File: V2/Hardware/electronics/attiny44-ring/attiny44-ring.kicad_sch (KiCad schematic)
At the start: 16 parts, among them J1 CHAIN_IN, J2 CHAIN_OUT, J3 28BYJ-48, J4 HOME_SENSOR, J5 AVR_ISP_2X3, J6 5V_INJECT, U1 ATtiny44A-SS, U2 ULN2003A

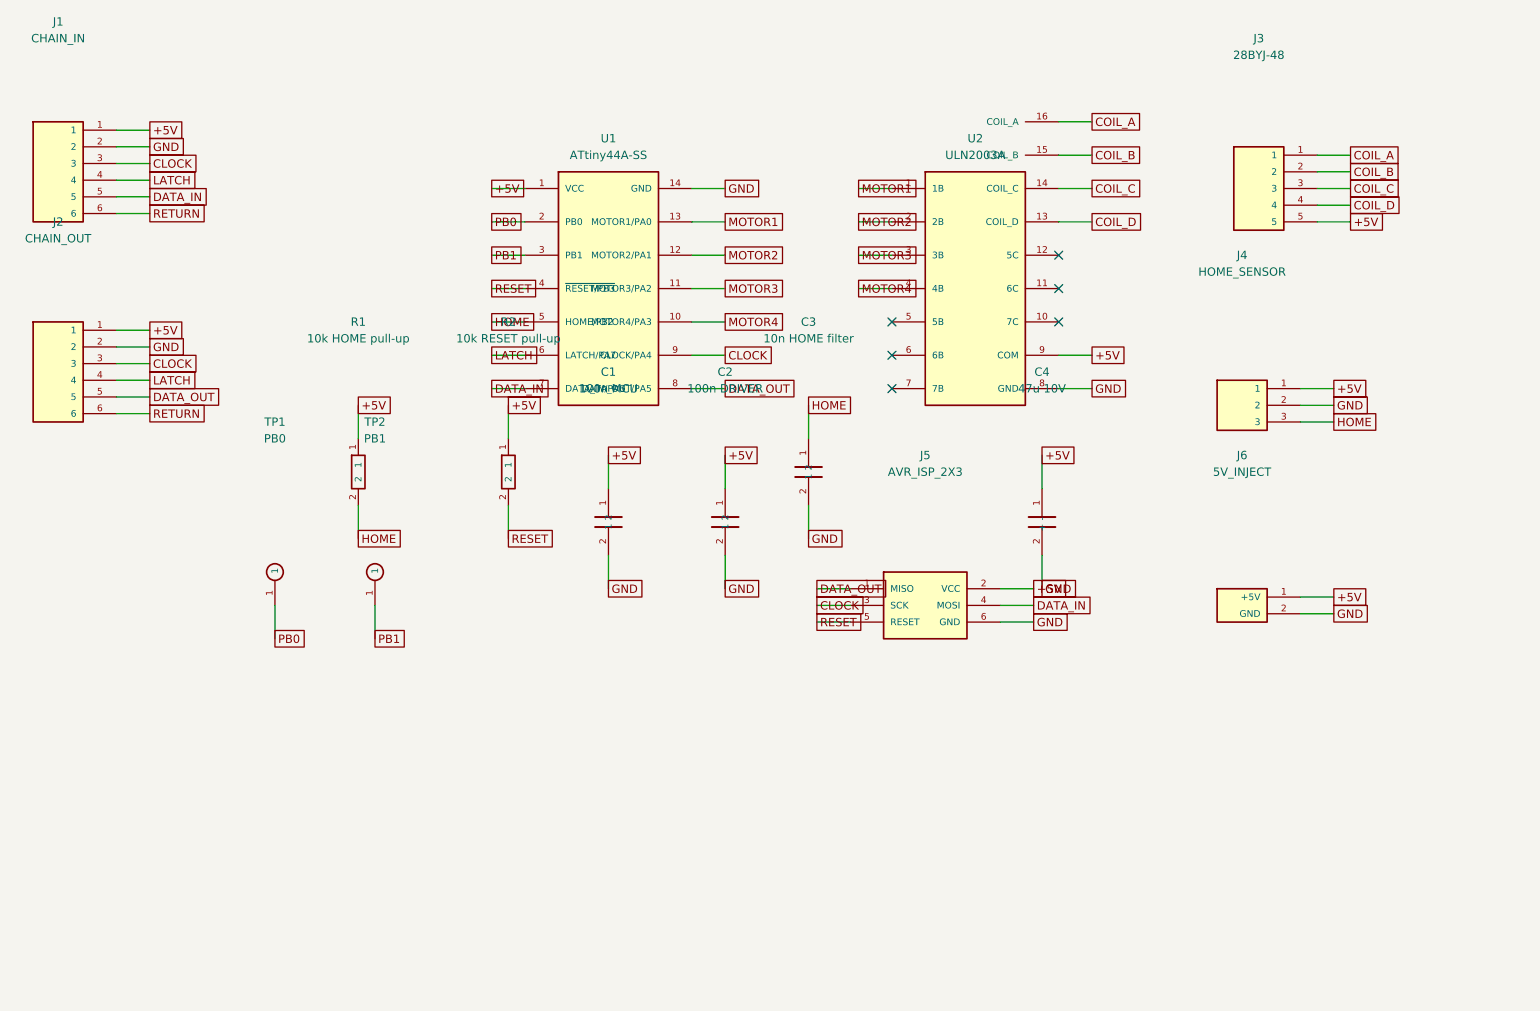
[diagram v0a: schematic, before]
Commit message: Redesign ATtiny44 ring board for milling
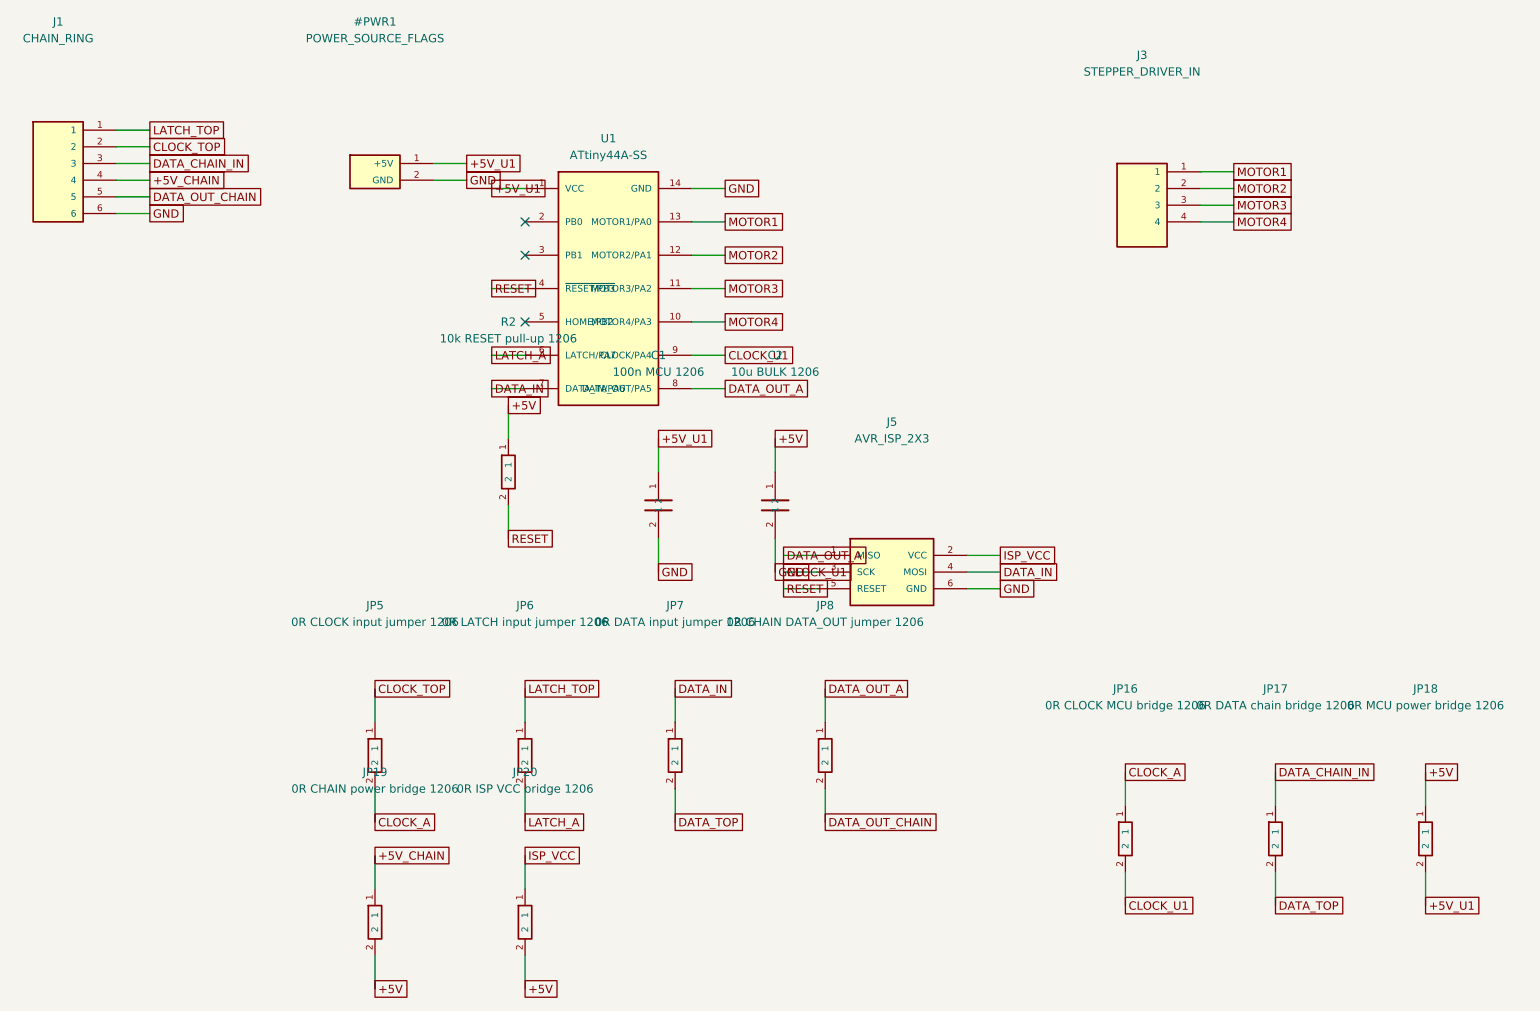
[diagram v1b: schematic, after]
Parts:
- removed C3: 10n HOME filter, Capacitor_SMD:C_0805_2012Metric_Pad1.18x1.45mm_HandSolder, symbol attiny44-ring:C
- removed C4: 47u 10V, Capacitor_THT:CP_Radial_D5.0mm_P2.00mm, symbol attiny44-ring:CP
- removed J2: CHAIN_OUT, Connector_JST:JST_XH_B6B-XH-A_1x06_P2.50mm_Vertical, symbol attiny44-ring:CONN6
- removed J4: HOME_SENSOR, Connector_JST:JST_XH_B3B-XH-A_1x03_P2.50mm_Vertical, symbol attiny44-ring:CONN3
- removed J6: 5V_INJECT, Connector_JST:JST_XH_B2B-XH-A_1x02_P2.50mm_Vertical, symbol attiny44-ring:CONN2
- removed R1: 10k HOME pull-up, Resistor_SMD:R_0805_2012Metric_Pad1.20x1.40mm_HandSolder, symbol attiny44-ring:R
- removed TP1: PB0, TestPoint:TestPoint_Plated_Hole_D2.0mm, symbol attiny44-ring:TESTPOINT
- removed TP2: PB1, TestPoint:TestPoint_Plated_Hole_D2.0mm, symbol attiny44-ring:TESTPOINT
- removed U2: ULN2003A, Package_SO:SOIC-16_3.9x9.9mm_P1.27mm, symbol attiny44-ring:ULN2003A
- added #PWR1: POWER_SOURCE_FLAGS, symbol attiny44-ring:CONN2
- added JP16: 0R CLOCK MCU bridge 1206, Resistor_SMD:R_1206_3216Metric_Pad1.30x1.75mm_HandSolder, symbol attiny44-ring:R
- added JP17: 0R DATA chain bridge 1206, Resistor_SMD:R_1206_3216Metric_Pad1.30x1.75mm_HandSolder, symbol attiny44-ring:R
- added JP18: 0R MCU power bridge 1206, Resistor_SMD:R_1206_3216Metric_Pad1.30x1.75mm_HandSolder, symbol attiny44-ring:R
- added JP19: 0R CHAIN power bridge 1206, Resistor_SMD:R_1206_3216Metric_Pad1.30x1.75mm_HandSolder, symbol attiny44-ring:R
- added JP20: 0R ISP VCC bridge 1206, Resistor_SMD:R_1206_3216Metric_Pad1.30x1.75mm_HandSolder, symbol attiny44-ring:R
- added JP5: 0R CLOCK input jumper 1206, Resistor_SMD:R_1206_3216Metric_Pad1.30x1.75mm_HandSolder, symbol attiny44-ring:R
- added JP6: 0R LATCH input jumper 1206, Resistor_SMD:R_1206_3216Metric_Pad1.30x1.75mm_HandSolder, symbol attiny44-ring:R
- added JP7: 0R DATA input jumper 1206, Resistor_SMD:R_1206_3216Metric_Pad1.30x1.75mm_HandSolder, symbol attiny44-ring:R
- added JP8: 0R CHAIN DATA_OUT jumper 1206, Resistor_SMD:R_1206_3216Metric_Pad1.30x1.75mm_HandSolder, symbol attiny44-ring:R
- C1: value 100n MCU -> 100n MCU 1206; footprint Capacitor_SMD:C_0805_2012Metric_Pad1.18x1.45mm_HandSolder -> Capacitor_SMD:C_1206_3216Metric_Pad1.33x1.80mm_HandSolder
- C2: value 100n DRIVER -> 10u BULK 1206; footprint Capacitor_SMD:C_0805_2012Metric_Pad1.18x1.45mm_HandSolder -> Capacitor_SMD:C_1206_3216Metric_Pad1.33x1.80mm_HandSolder
- J1: value CHAIN_IN -> CHAIN_RING; footprint Connector_JST:JST_XH_B6B-XH-A_1x06_P2.50mm_Vertical -> Connector_PinHeader_2.54mm:PinHeader_2x03_P2.54mm_Vertical_SMD
- J3: value 28BYJ-48 -> STEPPER_DRIVER_IN; footprint Connector_JST:JST_XH_B5B-XH-A_1x05_P2.50mm_Vertical -> Connector_PinHeader_2.54mm:PinHeader_1x04_P2.54mm_Vertical_SMD_Pin1Left; symbol attiny44-ring:CONN5 -> attiny44-ring:CONN4
- J5: footprint Connector_IDC:IDC-Header_2x03_P2.54mm_Vertical -> Connector_PinHeader_2.54mm:PinHeader_2x03_P2.54mm_Vertical_SMD
- R2: value 10k RESET pull-up -> 10k RESET pull-up 1206; footprint Resistor_SMD:R_0805_2012Metric_Pad1.20x1.40mm_HandSolder -> Resistor_SMD:R_1206_3216Metric_Pad1.30x1.75mm_HandSolder
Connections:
- net COIL_A is gone; now on net MOTOR1: J3.1
- net COIL_B is gone; now on net MOTOR2: J3.2
- net COIL_C is gone; now on net MOTOR3: J3.3
- net COIL_D is gone; now on net MOTOR4: J3.4
- net RETURN is gone; now on net GND: J1.6
- net +5V: now also JP18.1, JP19.2, JP20.2; no longer C1.1, J1.1, J3.5, J5.2 (VCC), U1.1 (VCC)
- net DATA_IN: now also JP7.1; no longer J1.5
- net GND: now also #PWR1.2 (GND); no longer J1.2
- net CLOCK renamed CLOCK_U1
- net CLOCK_U1: now also JP16.2; no longer J1.3
- net DATA_OUT renamed DATA_OUT_A
- net DATA_OUT_A: now also JP8.1
- net HOME: no longer names the net of U1.5 (HOME/PB2)
- net LATCH renamed +5V_CHAIN
- net +5V_CHAIN: now also JP19.1; no longer U1.6 (LATCH/PA7)
- net PB0: no longer names the net of U1.2 (PB0)
- net PB1: no longer names the net of U1.3 (PB1)
- new net +5V_U1: #PWR1.1 (+5V), C1.1, JP18.2, U1.1 (VCC)
- new net CLOCK_A: JP16.1, JP5.2
- new net CLOCK_TOP: J1.2, JP5.1
- new net DATA_CHAIN_IN: J1.3, JP17.1
- new net DATA_OUT_CHAIN: J1.5, JP8.2
- new net DATA_TOP: JP17.2, JP7.2
- new net ISP_VCC: J5.2 (VCC), JP20.1
- new net LATCH_A: JP6.2, U1.6 (LATCH/PA7)
- new net LATCH_TOP: J1.1, JP6.1
- no-connect marks 6 -> 3
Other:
- title: Alphabets V2 ATtiny44 SPI ring module -> Alphabets V2 ATtiny44 millable ring module
- moved on the sheet: C1, C2, J5

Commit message: Compact ATtiny44 ring PCB to 50x57 mm
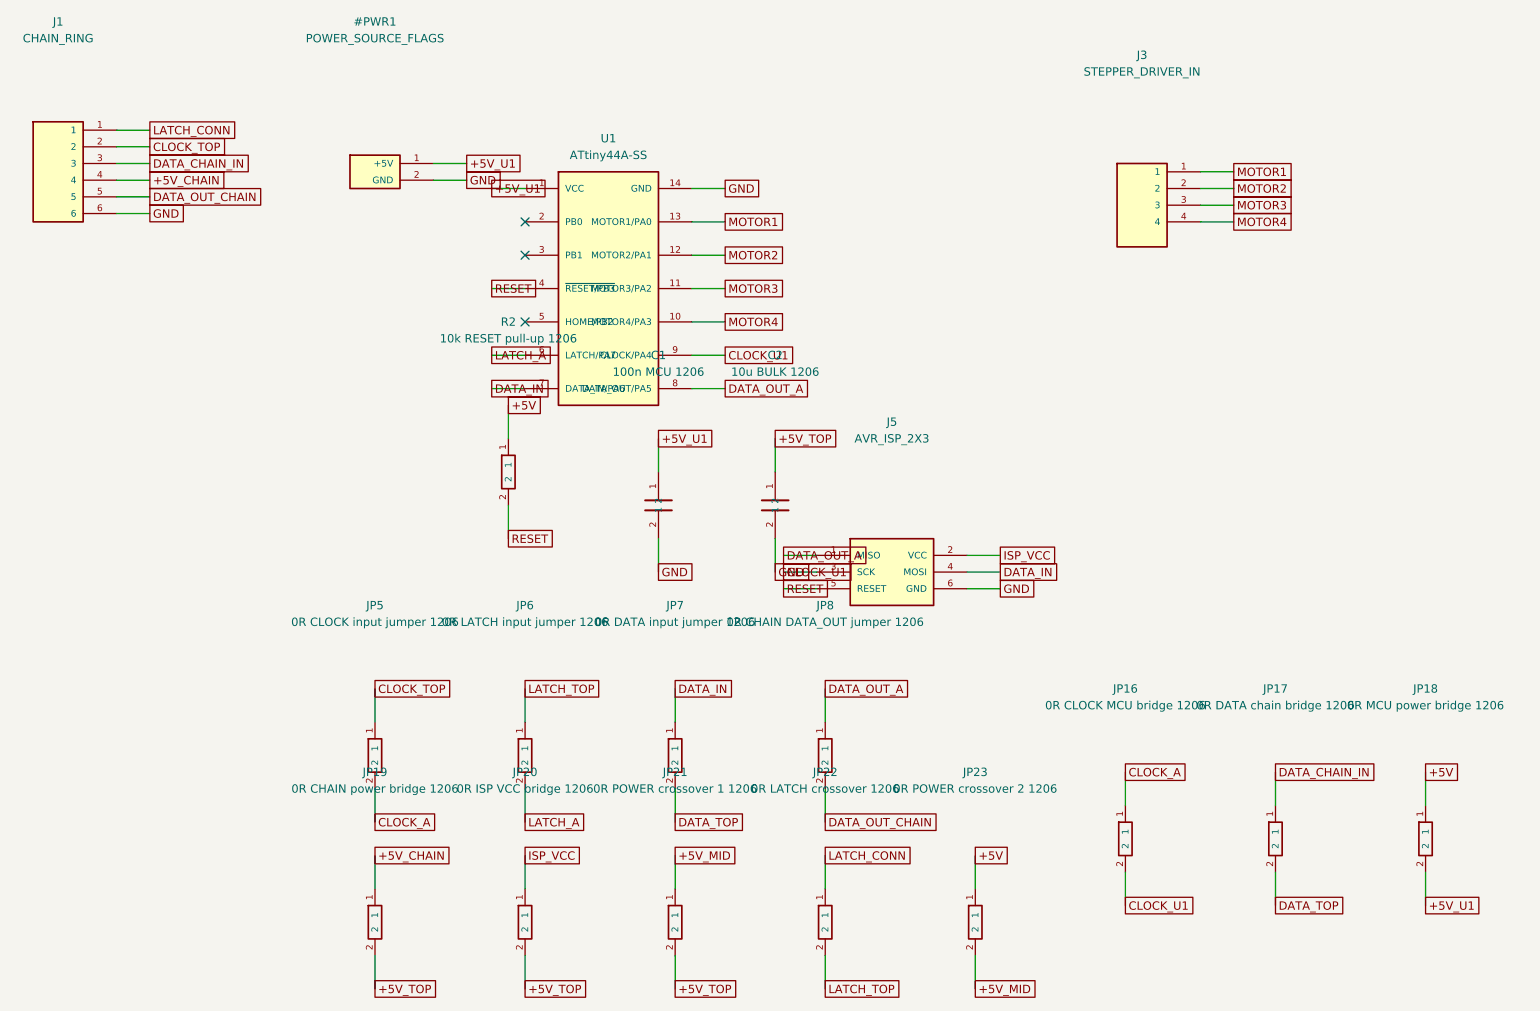
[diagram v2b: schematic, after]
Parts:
- added JP21: 0R POWER crossover 1 1206, Alphabets:R_1206_3216Metric_CompactCrossover, symbol attiny44-ring:R
- added JP22: 0R LATCH crossover 1206, Alphabets:R_1206_3216Metric_CompactCrossover, symbol attiny44-ring:R
- added JP23: 0R POWER crossover 2 1206, Alphabets:R_1206_3216Metric_CompactCrossover, symbol attiny44-ring:R
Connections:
- net +5V: now also JP23.1; no longer C2.1, JP19.2, JP20.2
- net LATCH_TOP: now also JP22.2; no longer J1.1
- new net +5V_MID: JP21.1, JP23.2
- new net +5V_TOP: C2.1, JP19.2, JP20.2, JP21.2
- new net LATCH_CONN: J1.1, JP22.1

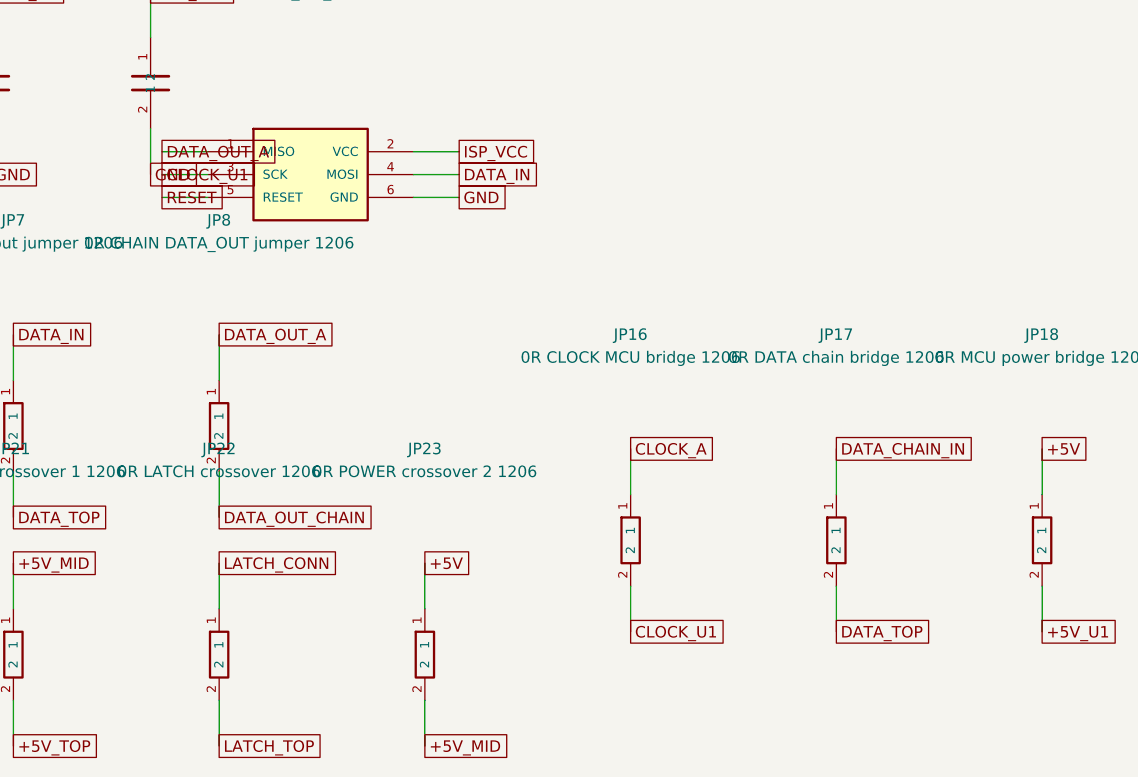
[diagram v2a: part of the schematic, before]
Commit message: Place ISP beside ATtiny44 on compact board
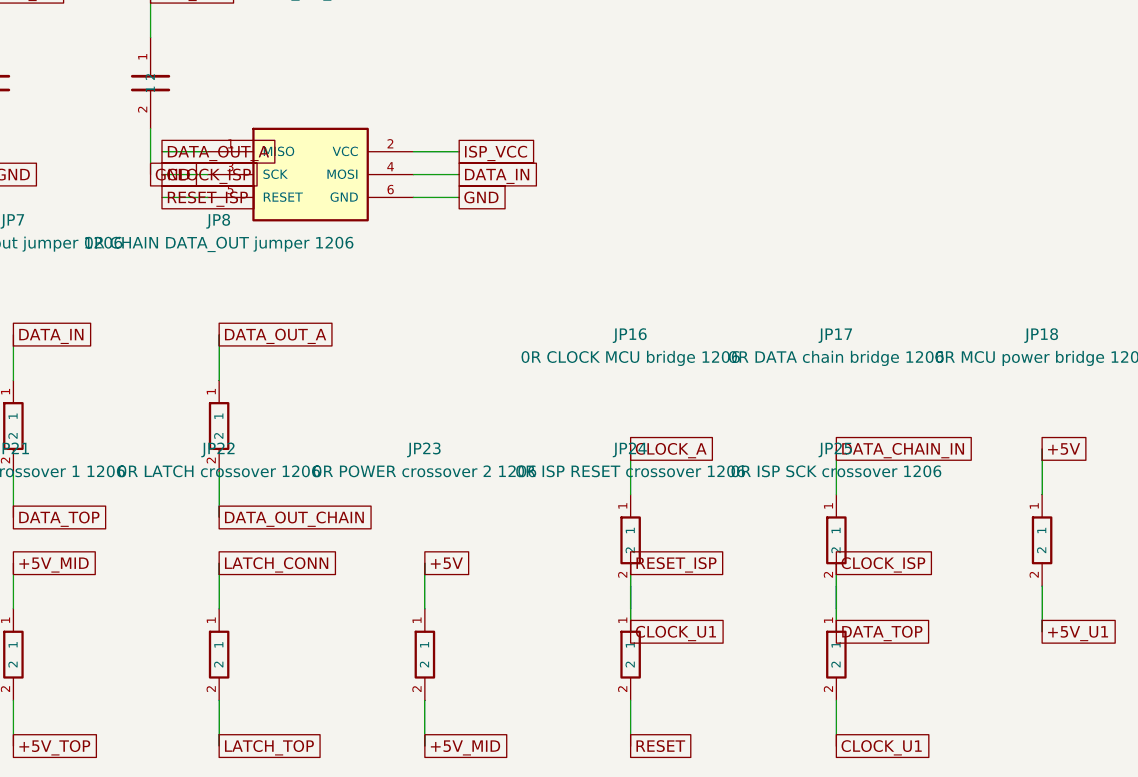
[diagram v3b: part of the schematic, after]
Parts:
- added JP24: 0R ISP RESET crossover 1206, Alphabets:R_1206_3216Metric_CompactCrossover, symbol attiny44-ring:R
- added JP25: 0R ISP SCK crossover 1206, Alphabets:R_1206_3216Metric_CompactCrossover, symbol attiny44-ring:R
- JP20: footprint Resistor_SMD:R_1206_3216Metric_Pad1.30x1.75mm_HandSolder -> Alphabets:R_1206_3216Metric_CompactCrossover
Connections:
- net CLOCK_U1: now also J5.5 (RESET), JP24.1, JP25.2; no longer J5.3 (SCK)
- net RESET: now also JP24.2; no longer J5.5 (RESET)
- net DATA_TOP renamed CLOCK_ISP
- net CLOCK_ISP: now also J5.3 (SCK), JP25.1
